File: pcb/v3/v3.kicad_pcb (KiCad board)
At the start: 2 copper layers, 100 x 100 mm, 48 parts, among them J1 RJ10, J10 USB_A, J2 ICSP, J3 RJ10, J4 RJ10, J5 RJ10, J6 RJ10, J7 RJ10, J8 BOOST, J9 USB_B, Q2 2N3904, Q3 BS170, SW1 CTL1, SW2 CTL2, SW3 CTL3, U1 ATmega328P-PU, U2 PCF8574, U3 RC1602A, Y1 16MHz

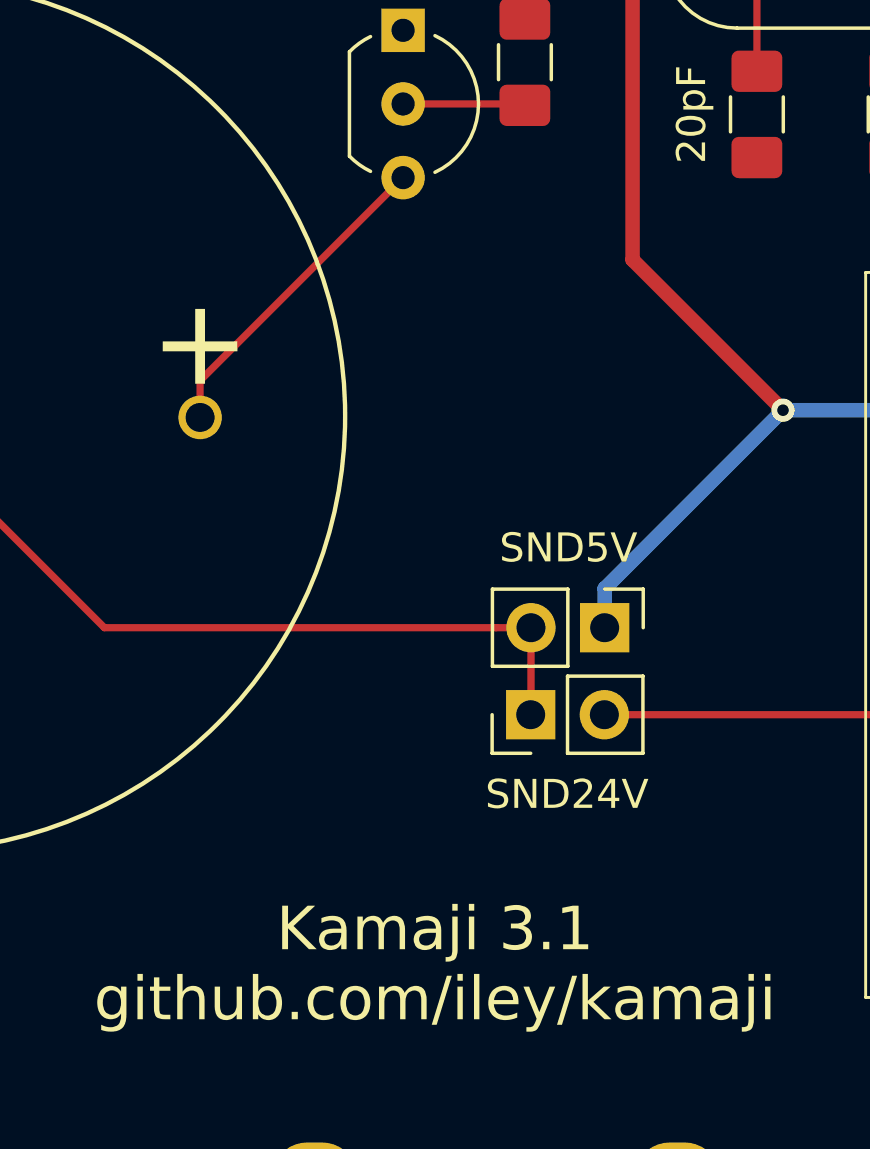
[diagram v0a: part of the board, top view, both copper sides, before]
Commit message: add a capacitor to fix sound
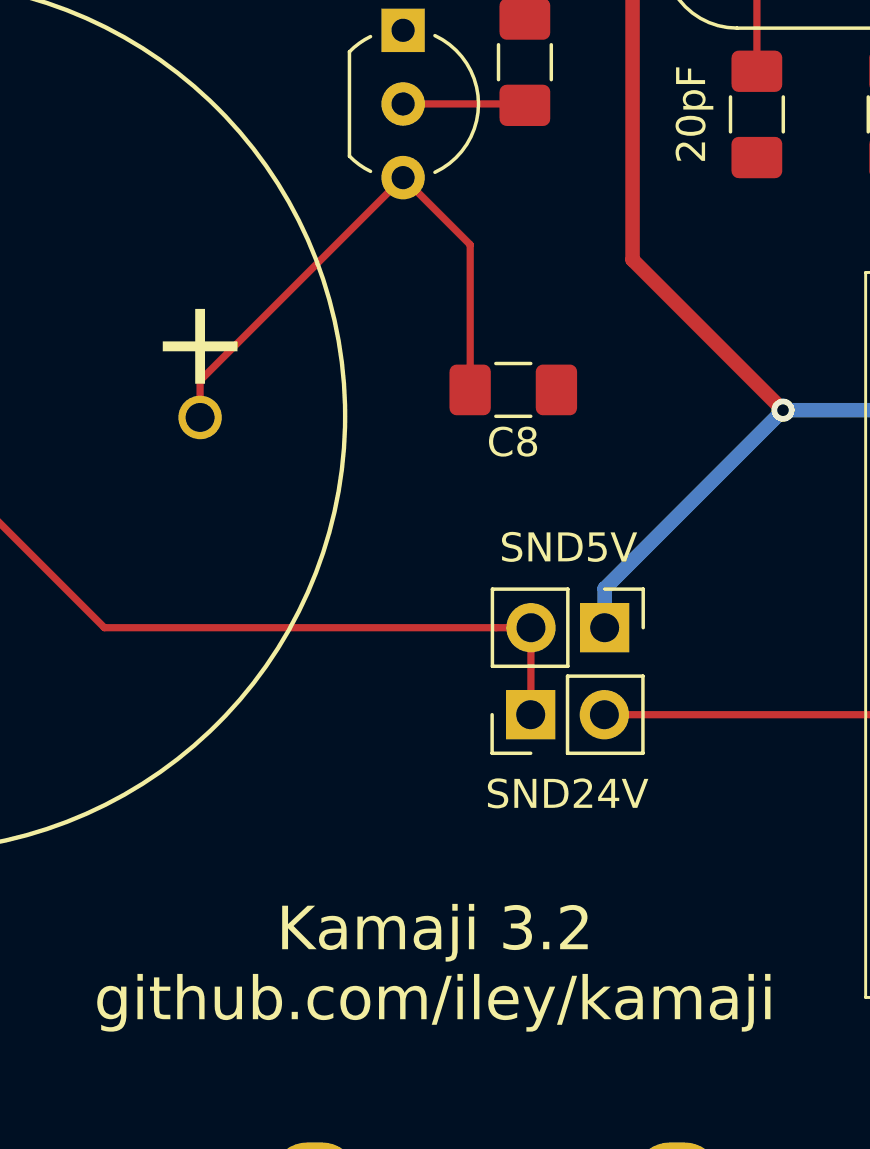
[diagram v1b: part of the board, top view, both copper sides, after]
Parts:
- added C8: 10uF, Capacitor_SMD:C_1206_3216Metric_Pad1.42x1.75mm_HandSolder, F.Cu at (100.6, 110.3)
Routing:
- net Net-(C8-Pad2): track 11.2 -> 19.4 mm
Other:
- board text added: "Kamaji 3.2 github.com/iley/kamaji"
- board text removed: "Kamaji 3.1 github.com/iley/kamaji"
